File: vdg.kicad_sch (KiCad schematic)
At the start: 3 parts, among them IC12 MC6847, IC13 74LS273N

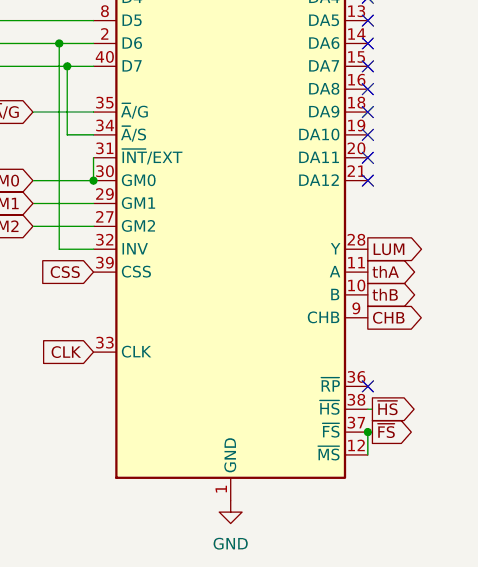
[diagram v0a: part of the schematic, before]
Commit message: fix video circuit gnd
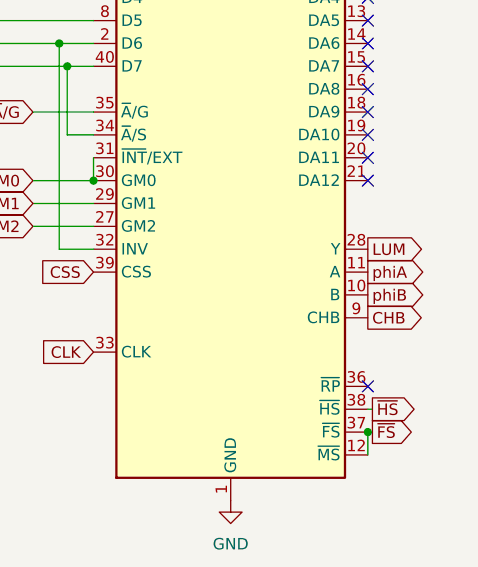
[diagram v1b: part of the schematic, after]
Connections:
- net thA renamed phiA
- net thB renamed phiB
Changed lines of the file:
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@@
     )
   )
-  (global_label "thA" (shape output) (at 177.8 111.252 0) (fields_autoplaced)
+  (global_label "phiA" (shape output) (at 177.8 111.252 0) (fields_autoplaced)
     (effects (font (size 1.27 1.27)) (justify left))
-    (property "Intersheet References" "${INTERSHEET_REFS}" (id 0) (at 183.0875 111.1726 0)
+    (property "Intersheet References" "${INTERSHEET_REFS}" (id 0) (at 184.1156 111.1726 0)
       (effects (font (size 1.27 1.27)) (justify left) hide)
     )
@@
     )
   )
-  (global_label "thB" (shape output) (at 177.8 113.792 0) (fields_autoplaced)
+  (global_label "phiB" (shape output) (at 177.8 113.792 0) (fields_autoplaced)
     (effects (font (size 1.27 1.27)) (justify left))
-    (property "Intersheet References" "${INTERSHEET_REFS}" (id 0) (at 183.269 113.7126 0)
+    (property "Intersheet References" "${INTERSHEET_REFS}" (id 0) (at 184.2971 113.7126 0)
       (effects (font (size 1.27 1.27)) (justify left) hide)
     )

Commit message: refresh pcb
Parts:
- IC12, IC13: SA2120 (none) -> Sheet 1
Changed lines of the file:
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@@
+      (effects (font (size 1.27 1.27)) hide)
+    )
+    (property "SA2120" "Sheet 1" (id 6) (at 111.252 83.312 0)
       (effects (font (size 1.27 1.27)) hide)
     )
@@
       (effects (font (size 1.27 1.27)) hide)
     )
+    (property "SA2120" "Sheet 1" (id 5) (at 162.56 101.092 0)
+      (effects (font (size 1.27 1.27)) hide)
+    )
